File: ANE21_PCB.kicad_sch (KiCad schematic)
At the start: 8 parts

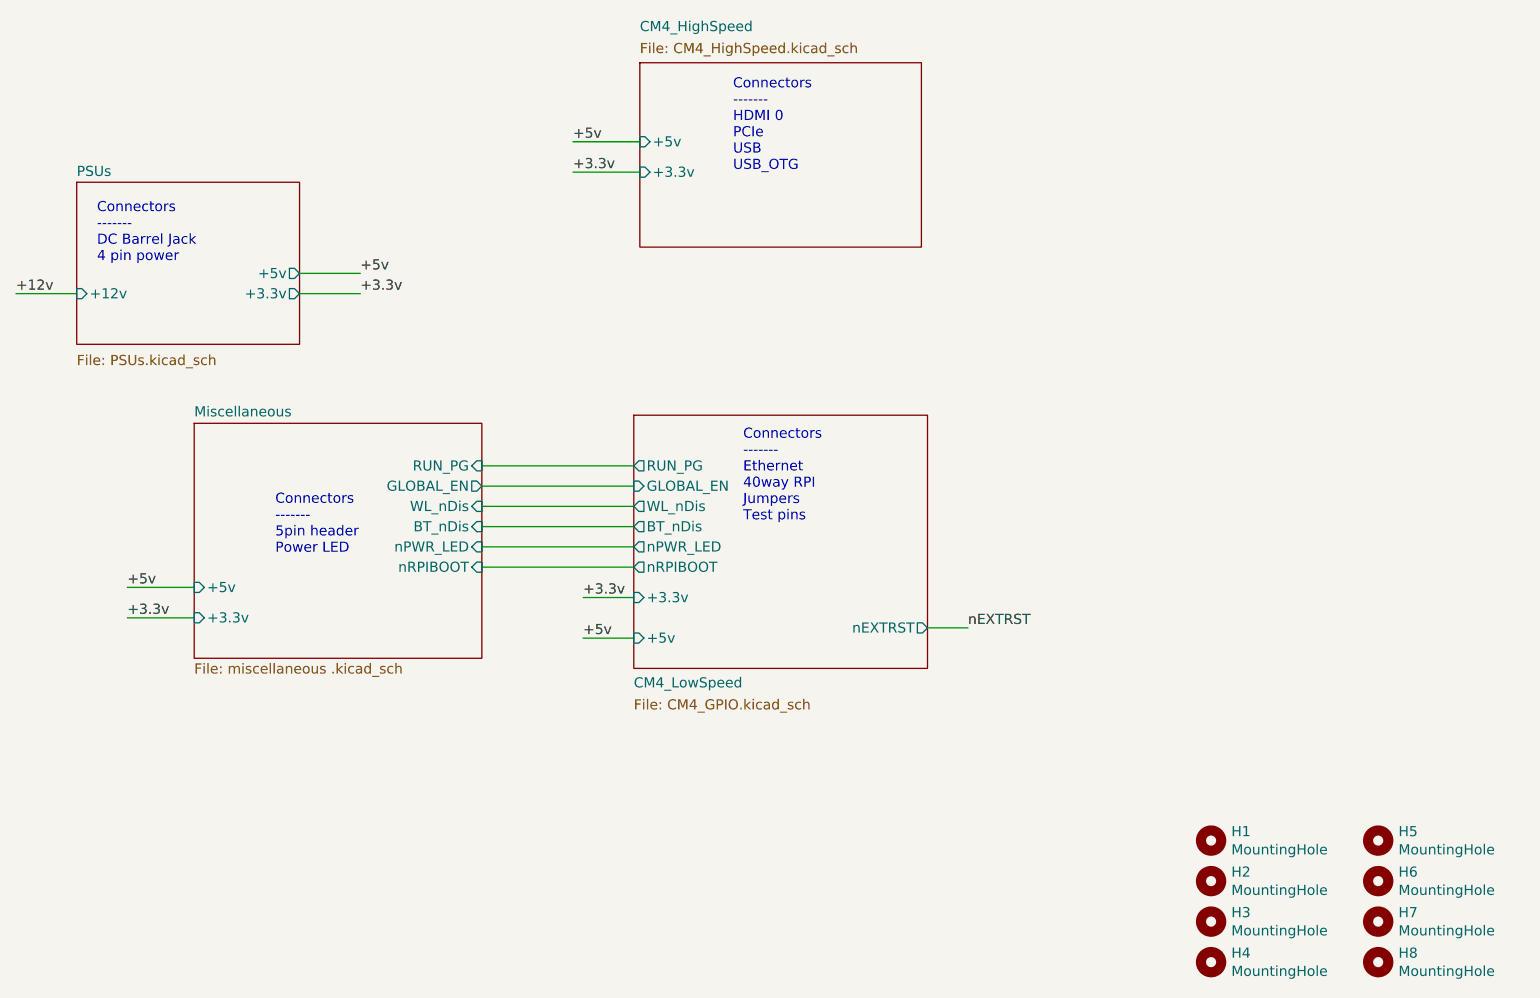
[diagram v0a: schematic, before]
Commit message: Redid traces with correct requirements, needs double checking.
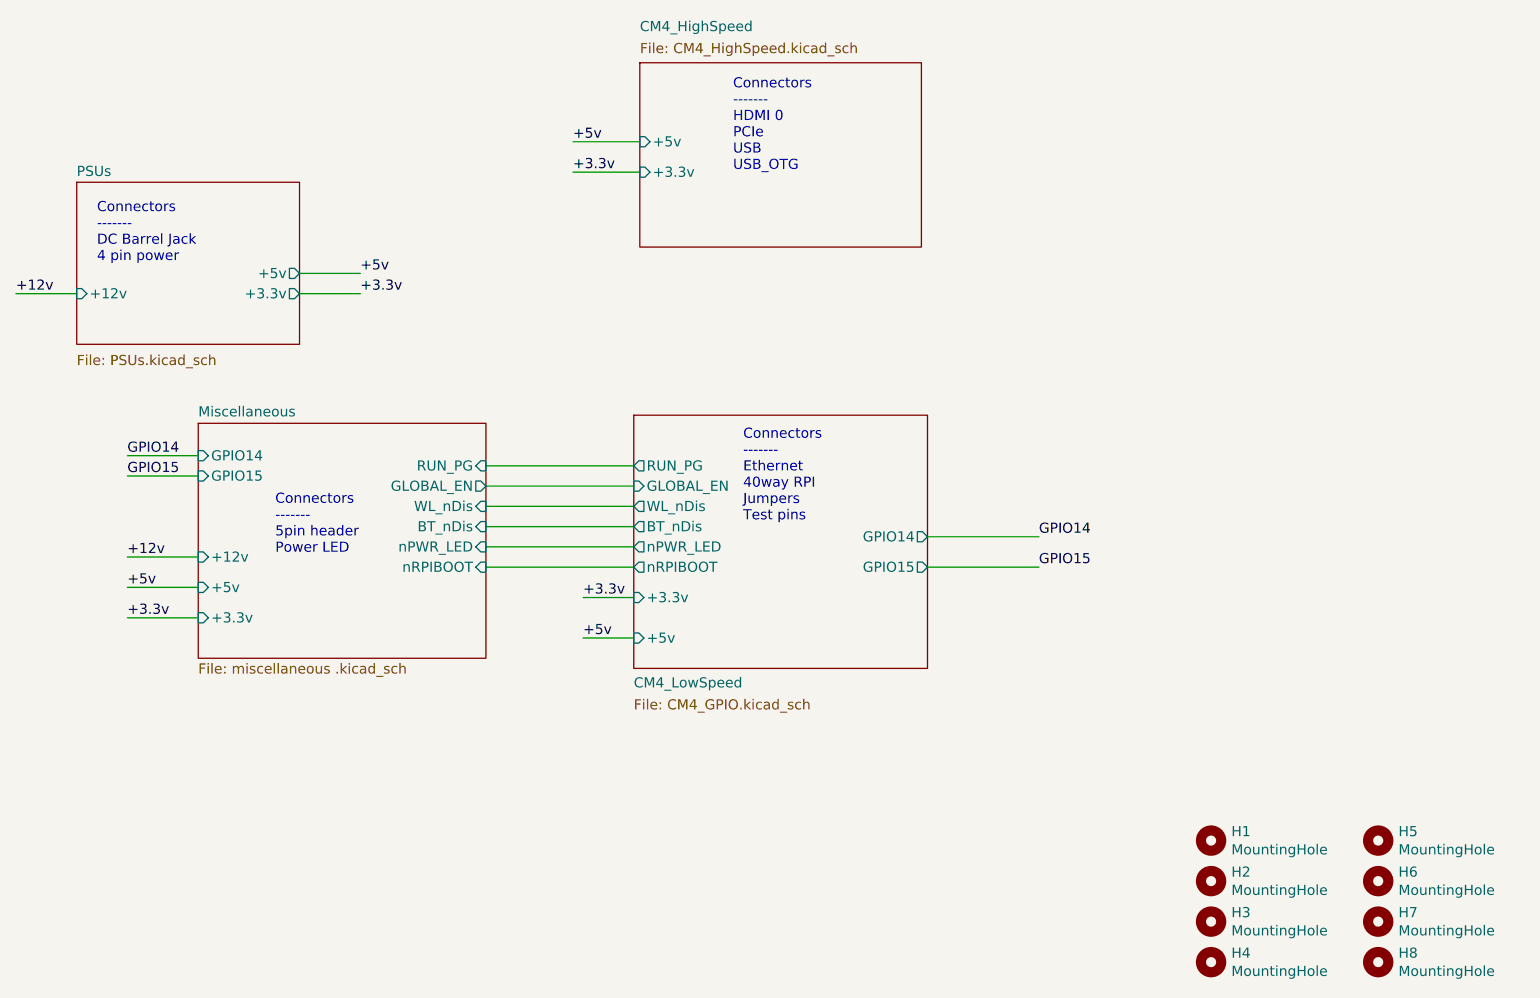
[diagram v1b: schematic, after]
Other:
- sheet CM4_LowSpeed ports: added GPIO14, GPIO15; removed nEXTRST
- sheet Miscellaneous ports: added +12v, GPIO14, GPIO15; removed none
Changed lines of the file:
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@@
 	(wire
 		(pts
-			(xy 43.18 115.57) (xy 51.562 115.57)
+			(xy 43.18 101.6) (xy 52.07 101.6)
+		)
+		(stroke
+			(width 0)
+			(type default)
+		)
+	)
+	(wire
+		(pts
+			(xy 43.18 115.57) (xy 52.07 115.57)
+		)
+		(stroke
+			(width 0)
+			(type default)
+		)
+	)
+	(wire
+		(pts
+			(xy 43.18 111.76) (xy 52.07 111.76)
 		)
 		(stroke
@@
 	(wire
 		(pts
-			(xy 87.63 110.49) (xy 106.68 110.49)
-		)
-		(stroke
-			(width 0)
-			(type default)
-		)
-	)
-	(wire
-		(pts
-			(xy 87.63 100.33) (xy 106.68 100.33)
+			(xy 88.138 110.49) (xy 106.68 110.49)
+		)
+		(stroke
+			(width 0)
+			(type default)
+		)
+	)
+	(wire
+		(pts
+			(xy 143.51 109.22) (xy 157.48 109.22)
+		)
+		(stroke
+			(width 0)
+			(type default)
+		)
+	)
+	(wire
+		(pts
+			(xy 88.138 100.33) (xy 106.68 100.33)
 		)
 		(stroke
@@
 	(wire
 		(pts
-			(xy 143.51 120.65) (xy 148.59 120.65)
-		)
-		(stroke
-			(width 0)
-			(type default)
-		)
-	)
-	(wire
-		(pts
 			(xy 64.77 76.2) (xy 72.39 76.2)
 		)
@@
 	(wire
 		(pts
-			(xy 87.63 113.03) (xy 106.68 113.03)
+			(xy 88.138 113.03) (xy 106.68 113.03)
 		)
 		(stroke
@@
 	(wire
 		(pts
-			(xy 87.63 107.95) (xy 106.68 107.95)
-		)
-		(stroke
-			(width 0)
-			(type default)
-		)
-	)
-	(wire
-		(pts
-			(xy 43.18 119.38) (xy 51.562 119.38)
+			(xy 88.138 107.95) (xy 106.68 107.95)
+		)
+		(stroke
+			(width 0)
+			(type default)
+		)
+	)
+	(wire
+		(pts
+			(xy 43.18 119.38) (xy 52.07 119.38)
+		)
+		(stroke
+			(width 0)
+			(type default)
+		)
+	)
+	(wire
+		(pts
+			(xy 43.18 99.06) (xy 52.07 99.06)
+		)
+		(stroke
+			(width 0)
+			(type default)
+		)
+	)
+	(wire
+		(pts
+			(xy 143.51 113.03) (xy 157.48 113.03)
 		)
 		(stroke
@@
 	(wire
 		(pts
-			(xy 87.63 102.87) (xy 106.68 102.87)
-		)
-		(stroke
-			(width 0)
-			(type default)
-		)
-	)
-	(wire
-		(pts
-			(xy 87.63 105.41) (xy 106.68 105.41)
+			(xy 88.138 102.87) (xy 106.68 102.87)
+		)
+		(stroke
+			(width 0)
+			(type default)
+		)
+	)
+	(wire
+		(pts
+			(xy 88.138 105.41) (xy 106.68 105.41)
 		)
 		(stroke
@@
 		)
 	)
+	(label "GPIO14"
+		(at 43.18 99.06 0)
+		(effects
+			(font
+				(size 1.27 1.27)
+			)
+			(justify left bottom)
+		)
+	)
+	(label "GPIO15"
+		(at 43.18 101.6 0)
+		(effects
+			(font
+				(size 1.27 1.27)
+			)
+			(justify left bottom)
+		)
+	)
+	(label "GPIO14"
+		(at 157.48 109.22 0)
+		(effects
+			(font
+				(size 1.27 1.27)
+			)
+			(justify left bottom)
+		)
+	)
 	(label "+5v"
 		(at 99.06 59.69 0)
@@
 		)
 	)
-	(label "nEXTRST"
-		(at 148.59 120.65 0)
-		(effects
-			(font
-				(size 1.27 1.27)
-			)
-			(justify left bottom)
-		)
-	)
 	(label "+3.3v"
 		(at 99.06 63.5 0)
@@
 		)
 	)
+	(label "GPIO15"
+		(at 157.48 113.03 0)
+		(effects
+			(font
+				(size 1.27 1.27)
+			)
+			(justify left bottom)
+		)
+	)
 	(label "+3.3v"
 		(at 72.39 78.74 0)
+		(effects
+			(font
+				(size 1.27 1.27)
+			)
+			(justify left bottom)
+		)
+	)
+	(label "+12v"
+		(at 43.18 111.76 0)
 		(effects
 			(font
@@
 	)
 	(sheet
-		(at 51.562 94.996)
+		(at 52.07 94.996)
 		(size 36.068 29.464)
 		(exclude_from_sim no)
@@
 		)
 		(property "Sheetname" "Miscellaneous"
-			(at 51.562 94.2844 0)
+			(at 52.07 94.2844 0)
 			(effects
 				(font
@@
 		)
 		(property "Sheetfile" "miscellaneous .kicad_sch"
-			(at 51.562 125.0446 0)
+			(at 52.07 125.0446 0)
 			(effects
 				(font
@@
 		)
 		(pin "BT_nDis" input
-			(at 87.63 107.95 0)
+			(at 88.138 107.95 0)
 			(effects
 				(font
@@
 		)
 		(pin "GLOBAL_EN" output
-			(at 87.63 102.87 0)
+			(at 88.138 102.87 0)
 			(effects
 				(font
@@
 		)
 		(pin "WL_nDis" input
-			(at 87.63 105.41 0)
+			(at 88.138 105.41 0)
 			(effects
 				(font
@@
 		)
 		(pin "nPWR_LED" input
-			(at 87.63 110.49 0)
+			(at 88.138 110.49 0)
 			(effects
 				(font
@@
 		)
 		(pin "nRPIBOOT" input
-			(at 87.63 113.03 0)
+			(at 88.138 113.03 0)
 			(effects
 				(font
@@
 		)
 		(pin "RUN_PG" input
-			(at 87.63 100.33 0)
+			(at 88.138 100.33 0)
 			(effects
 				(font
@@
 		)
 		(pin "+3.3v" input
-			(at 51.562 119.38 180)
+			(at 52.07 119.38 180)
 			(effects
 				(font
@@
 		)
 		(pin "+5v" input
-			(at 51.562 115.57 180)
+			(at 52.07 115.57 180)
+			(effects
+				(font
+					(size 1.27 1.27)
+				)
+				(justify left)
+			)
+		)
+		(pin "+12v" input
+			(at 52.07 111.76 180)
+			(effects
+				(font
+					(size 1.27 1.27)
+				)
+				(justify left)
+			)
+		)
+		(pin "GPIO14" input
+			(at 52.07 99.06 180)
+			(effects
+				(font
+					(size 1.27 1.27)
+				)
+				(justify left)
+			)
+		)
+		(pin "GPIO15" input
+			(at 52.07 101.6 180)
 			(effects
 				(font
@@
 			)
 		)
-		(pin "nEXTRST" output
-			(at 143.51 120.65 0)
-			(effects
-				(font
-					(size 1.27 1.27)
-				)
-				(justify right)
-			)
-		)
 		(pin "GLOBAL_EN" input
 			(at 106.68 102.87 180)
@@
 			)
 		)
+		(pin "GPIO14" output
+			(at 143.51 109.22 0)
+			(effects
+				(font
+					(size 1.27 1.27)
+				)
+				(justify right)
+			)
+		)
+		(pin "GPIO15" output
+			(at 143.51 113.03 0)
+			(effects
+				(font
+					(size 1.27 1.27)
+				)
+				(justify right)
+			)
+		)
